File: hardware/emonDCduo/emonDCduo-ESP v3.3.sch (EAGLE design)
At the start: 122 parts, among them P1 B4B-PH-K, Y1 32Khz

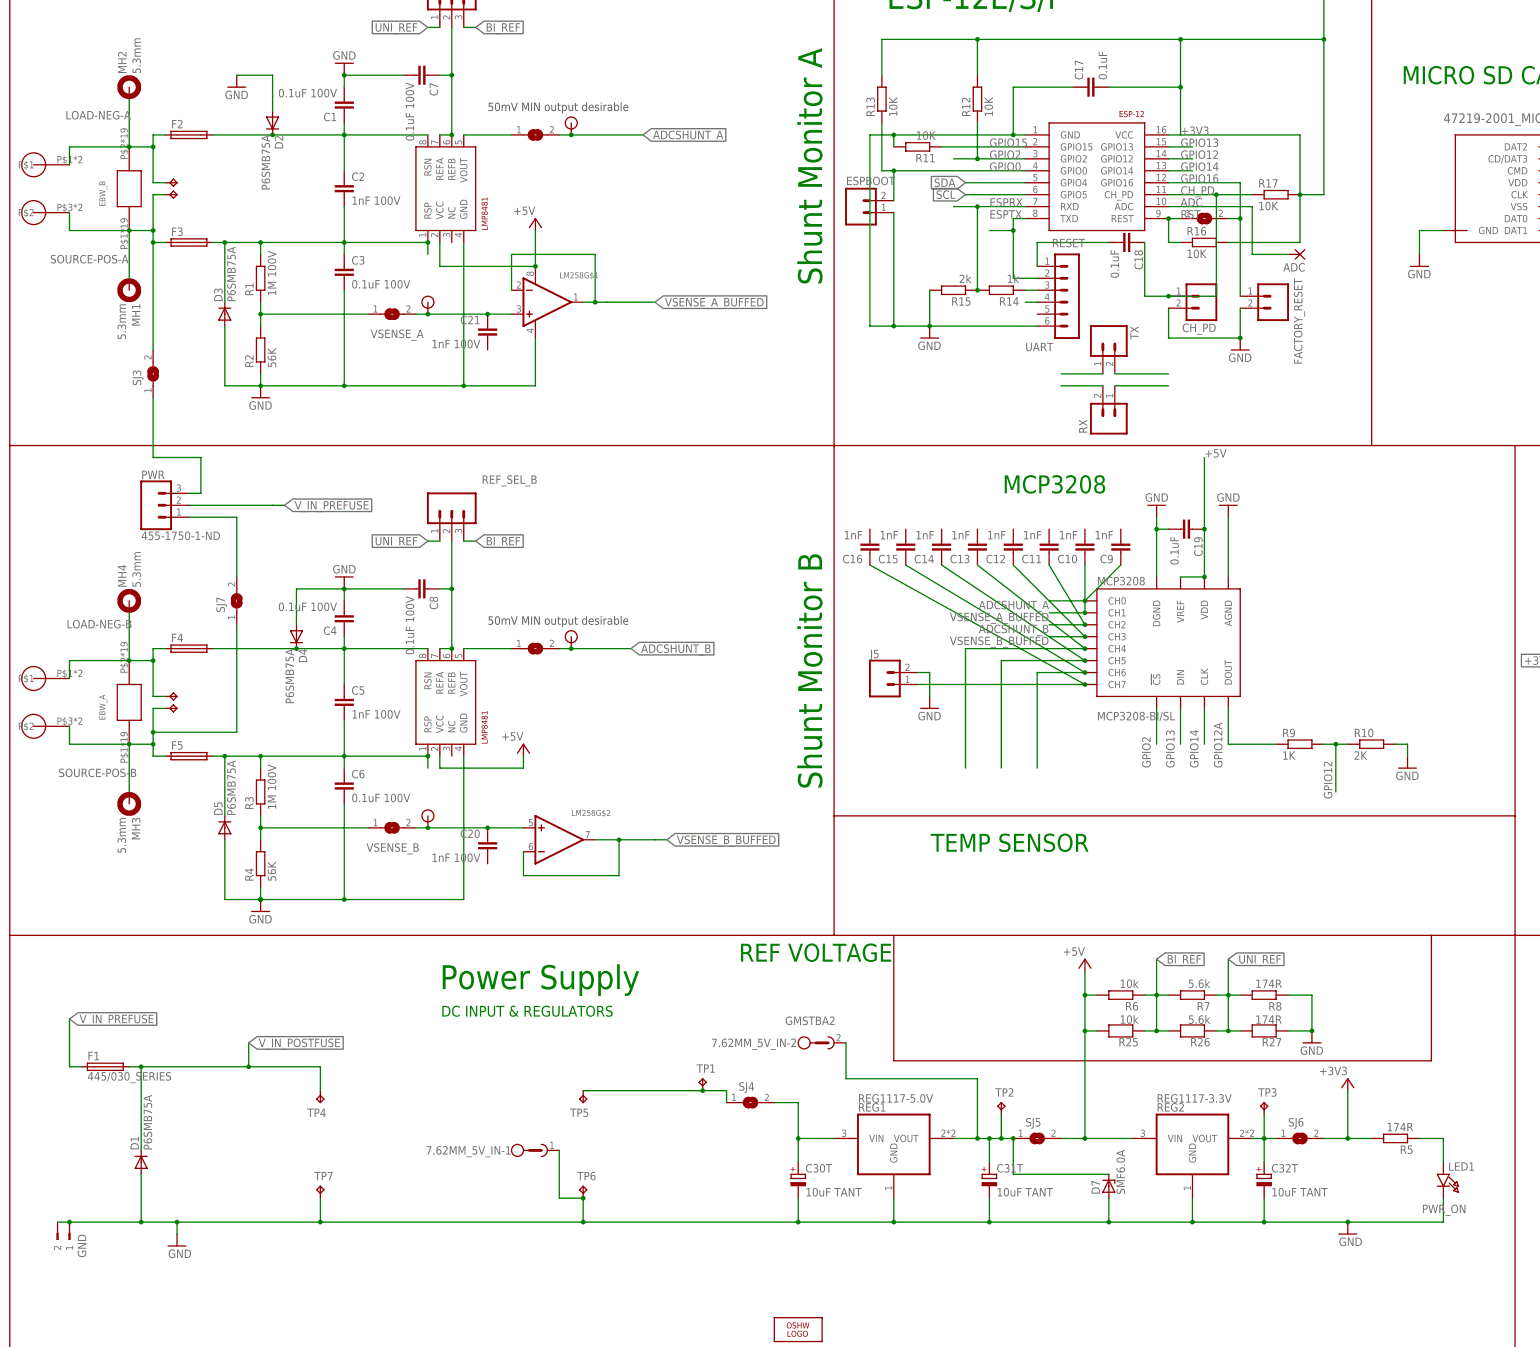
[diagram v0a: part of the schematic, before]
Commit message: commit v3.3
added temp sensor
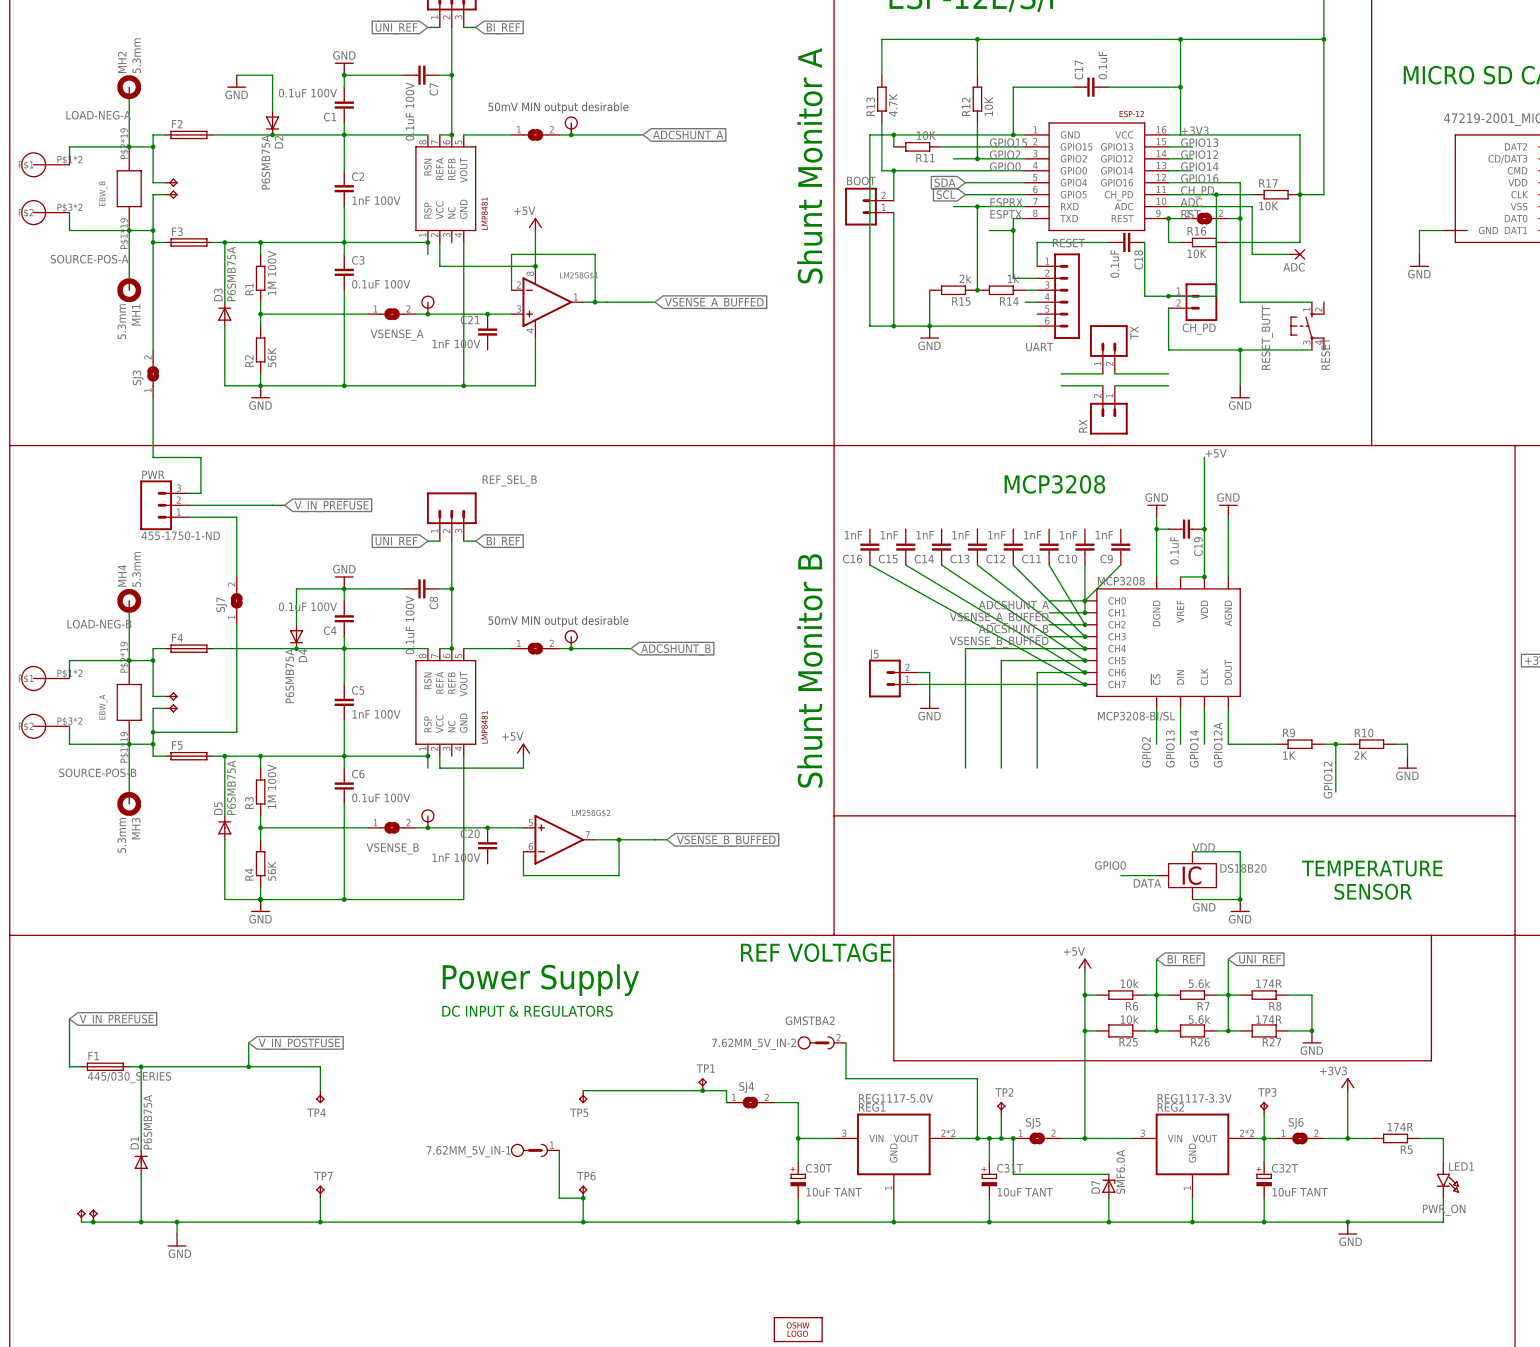
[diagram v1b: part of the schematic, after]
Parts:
- removed GND: (no value), con-weidmueller-sl35_db:180-2
- removed IO16: FACTORY_RESET, SparkFun:M02PTH
- added IC1: DS18B20, DS18B20:DS18B20
- added RESET: RESET_BUTT, switch-omron:10-XX
- added TP12, TP13: TPPAD1-13Y, testpad:TPPAD1-13Y
- R1, R2, R3, R4: device rcl7:R-EU_R0805 -> rcl7:R-EU_0207/2V
- R13: value 10K -> 4.7K
- renumbered ESPBOOT to BOOT
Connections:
- net GND: now also IC1.GND, IC1.VDD, RESET.P, TP12.TP, TP13.TP; no longer GND.1, GND.2, IO16.2
- net GPIO0: now also IC1.DATA
- net GPIO16: now also RESET.S; no longer IO16.1
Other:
- note added: "TEMPERATURE SENSOR"
- note removed: "TEMP SENSOR"
